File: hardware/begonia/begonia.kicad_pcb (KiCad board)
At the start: 2 copper layers, 70.7 x 53.3 mm, 11 parts, among them J1 NEIGHBOR1, J2 NEIGHBOR2, J7 BONUS_ROW, P1 POGOPINS, SW1 SPST

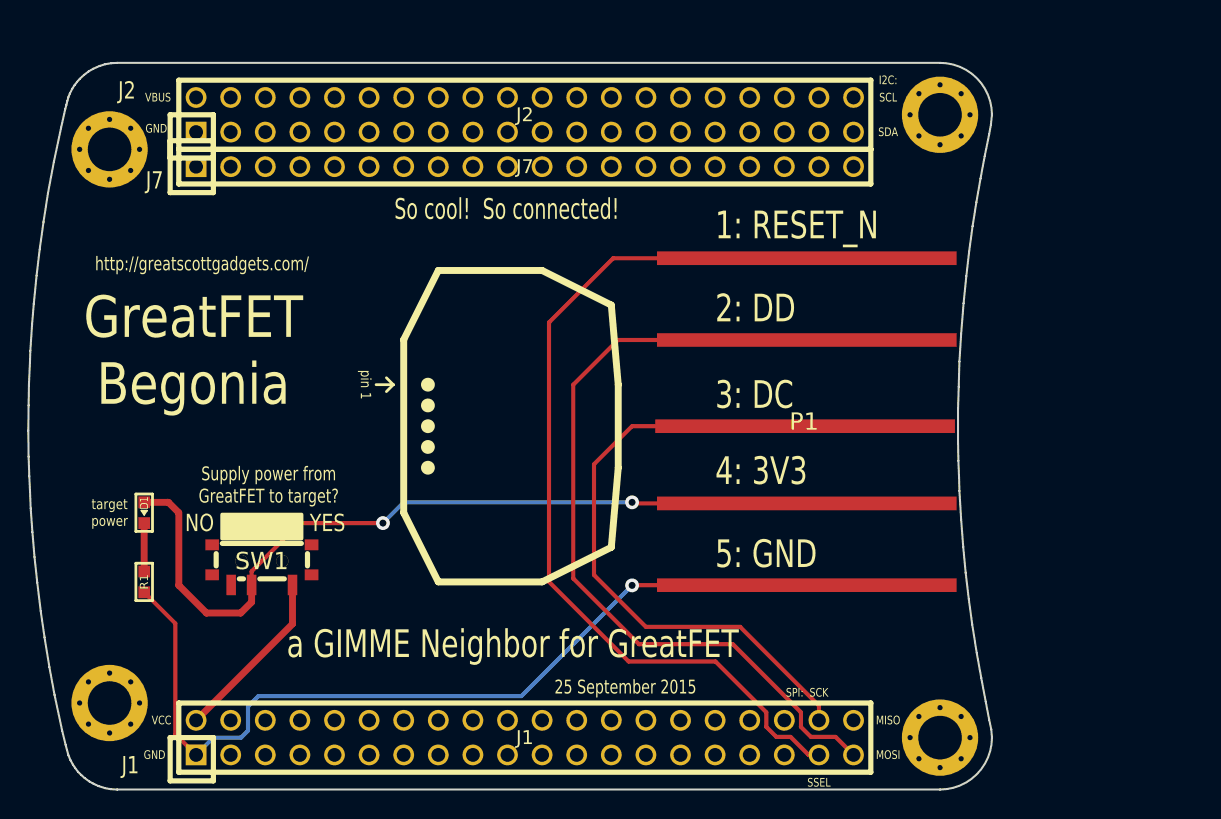
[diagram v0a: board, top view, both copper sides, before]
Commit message: crocus: added back mask layer
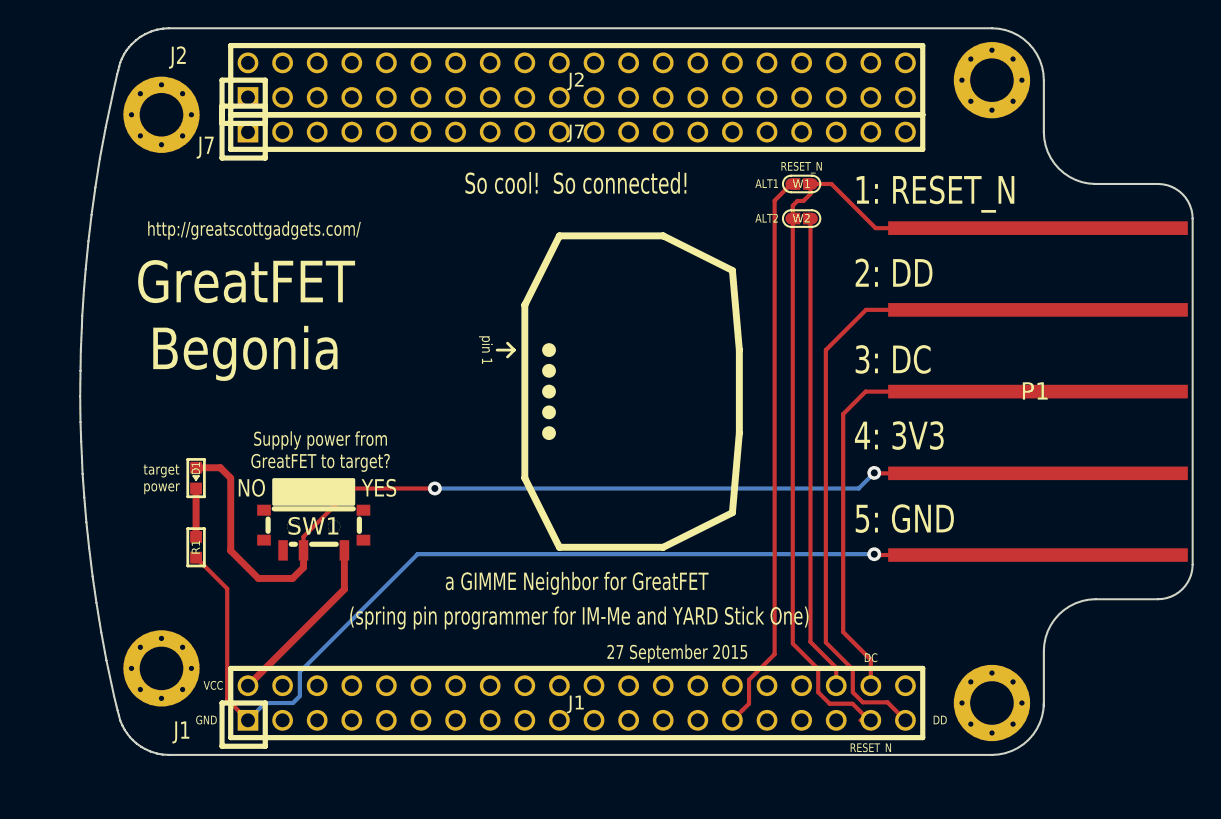
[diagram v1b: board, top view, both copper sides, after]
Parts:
- added W1: TEST, gsg-modules:0603-JUMPER, F.Cu at (162.6, 80.0)
- added W2: TEST, gsg-modules:0603-JUMPER, F.Cu at (162.6, 82.5)
- moved P1 17.1 mm to (168.9, 95.2)
- moved D1 4.58 mm to (118.1, 101.6)
- moved J1 4.58 mm to (146.1, 118.1)
- moved J2 4.58 mm to (146.1, 72.4)
- moved MH3 4.58 mm to (176.5, 118.1)
- moved MH4 4.58 mm to (176.5, 72.4)
- moved J7 4.58 mm to (146.1, 76.2)
- moved R1 4.58 mm to (118.1, 106.7)
- moved MH2 4.58 mm to (115.6, 115.6)
- moved MH1 4.58 mm to (115.6, 74.9)
- moved SW1 4.58 mm to (126.7, 105.2)
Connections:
- J1 pad 29: Net-(J1-Pad29) -> /RESET_N_ALT1
- J1 pad 36: Net-(J1-Pad36) -> /RESET_N_ALT2
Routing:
- net /RESET_N_ALT1: track 0.00 -> 41.3 mm
- net /RESET_N_ALT2: track 0.00 -> 35.1 mm
- net GND: track 64.6 -> 77.6 mm
- net +3V3: track 59.9 -> 72.8 mm
- net /DD: track 59.3 -> 47.4 mm
- net /DC: track 46.3 -> 35.8 mm
- net /RESET_N: track 65.6 -> 62.4 mm
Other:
- board size 70.7 x 53.3 mm -> 81.7 x 53.3 mm
- board text added: "(spring pin programmer for IM-Me and YARD Stick One)"
- board text added: "27 September 2015"
- board text added: "ALT1"
- board text added: "ALT2"
- board text added: "DC"
- board text added: "DD"
- board text added: "RESET_N"
- board text removed: "25 September 2015"
- board text removed: "I2C:"
- board text removed: "MISO"
- board text removed: "MOSI"
- board text removed: "SCK"
- board text removed: "SCL"
- board text removed: "SDA"
- board text removed: "SPI:"
- board text removed: "SSEL"
- board text removed: "VBUS"
